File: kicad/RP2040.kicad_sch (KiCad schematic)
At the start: 22 parts, among them J1 503398-1892, SW1 side-button, SW2 SKRPADE010, U2 RP2040

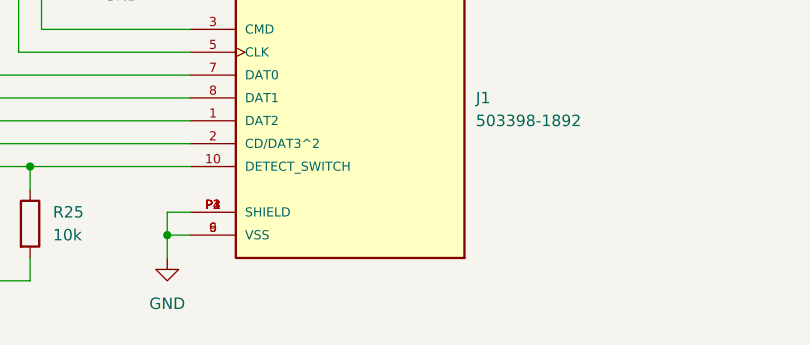
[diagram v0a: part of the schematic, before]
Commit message: added title to all circuit diagrams and sub-circuit diagrams, and PDF export
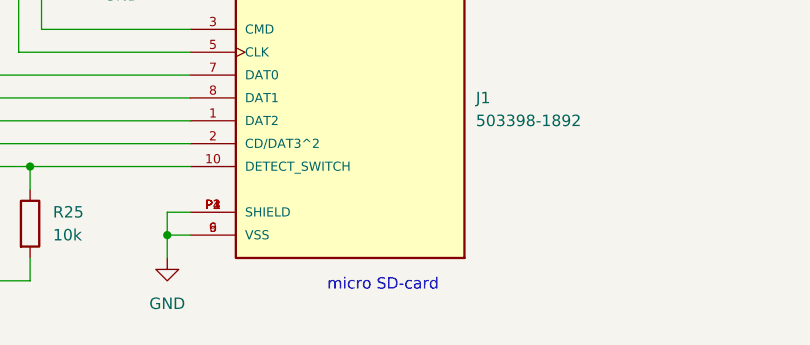
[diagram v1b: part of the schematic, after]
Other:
- note added: "micro SD-card"
- title: (none) -> RP2040 microcontroller
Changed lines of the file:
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@@
 (kicad_sch (version 20211123) (generator eeschema)
   (paper "A4")
+  (title_block
+    (title "RP2040 microcontroller")
+  )
   (junction (at 161.29 59.69) (diameter 0) (color 0 0 0 0)
   )
@@
     (stroke (width 0) (type default) (color 0 0 0 0))
   )
+  (text "micro SD-card" (at 205.74 152.4 0)
+    (effects (font (size 1.27 1.27)) (justify left bottom))
+  )
   (label "1.1V" (at 190.5 59.69 0)

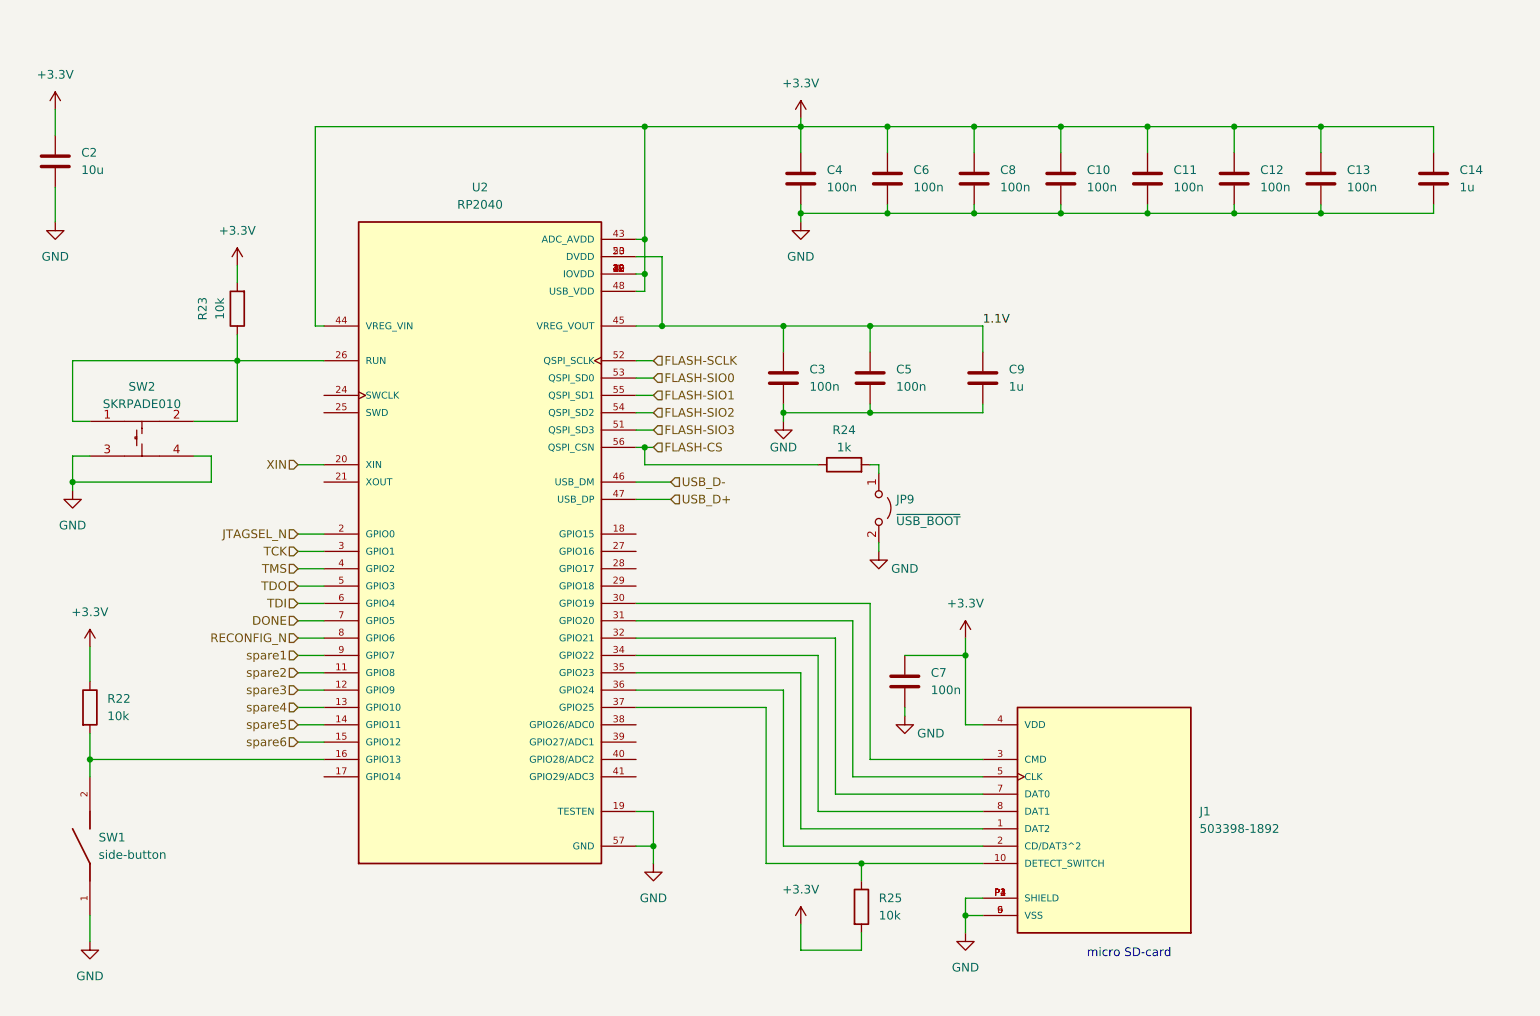
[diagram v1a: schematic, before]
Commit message: new flash, and IEC interface added
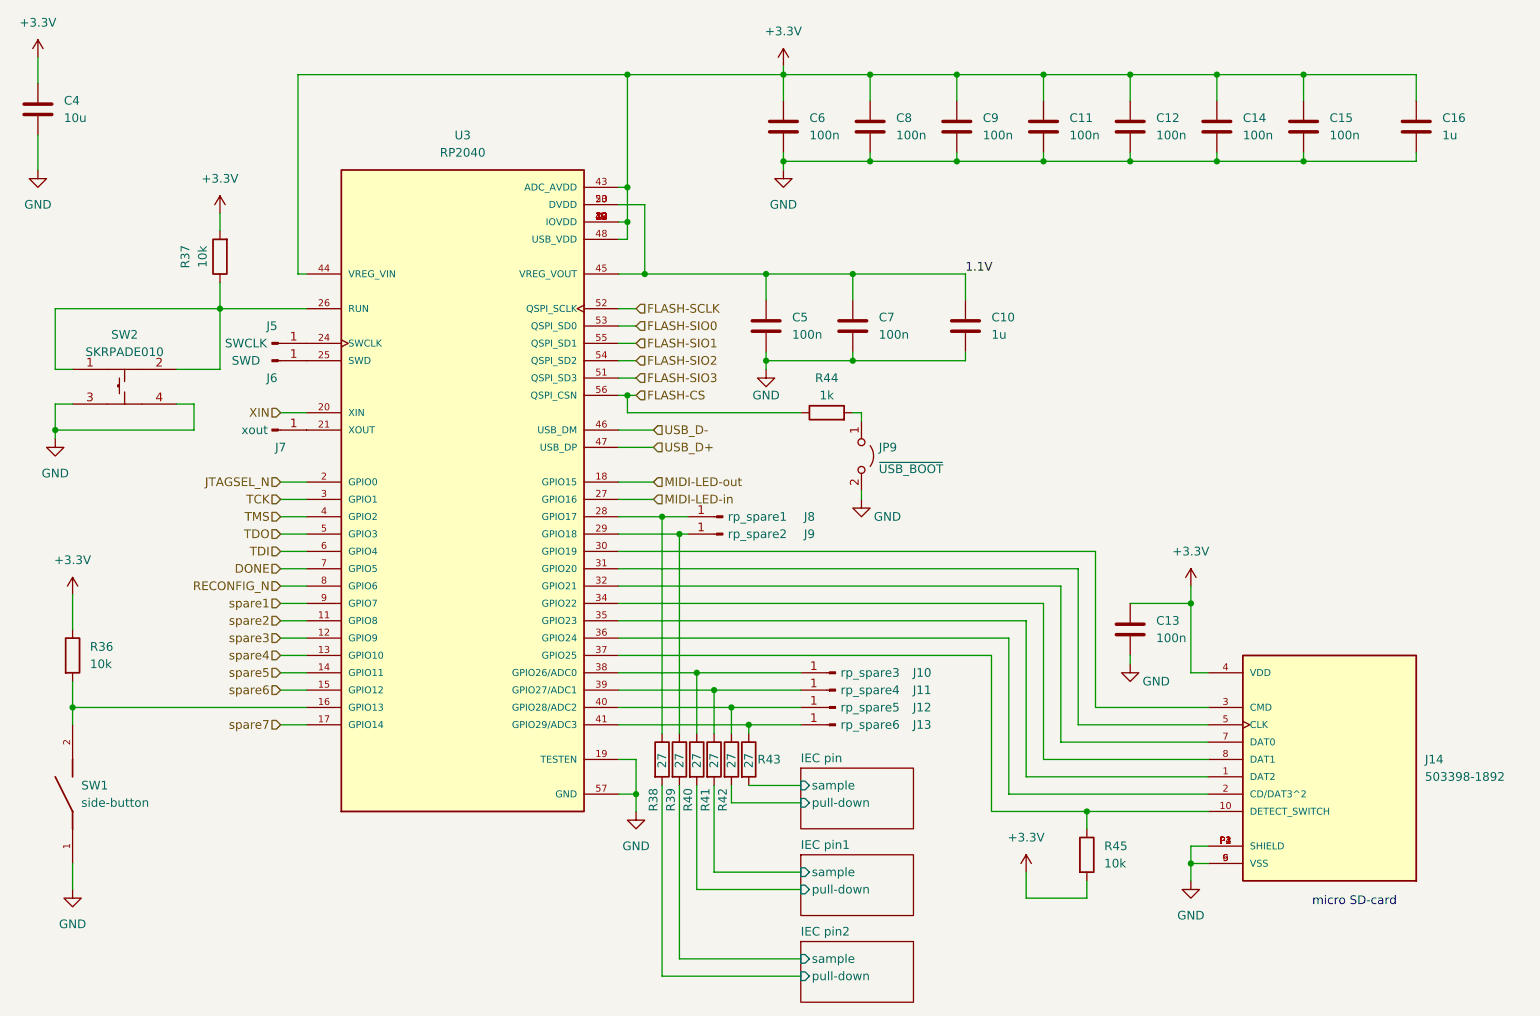
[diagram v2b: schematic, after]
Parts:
- added J10: rp_spare3, Connector_PinHeader_2.54mm:PinHeader_1x01_P2.54mm_Vertical, symbol Connector:Conn_01x01_Male
- added J11: rp_spare4, Connector_PinHeader_2.54mm:PinHeader_1x01_P2.54mm_Vertical, symbol Connector:Conn_01x01_Male
- added J12: rp_spare5, Connector_PinHeader_2.54mm:PinHeader_1x01_P2.54mm_Vertical, symbol Connector:Conn_01x01_Male
- added J13: rp_spare6, Connector_PinHeader_2.54mm:PinHeader_1x01_P2.54mm_Vertical, symbol Connector:Conn_01x01_Male
- added J5: SWCLK, Connector_PinHeader_2.54mm:PinHeader_1x01_P2.54mm_Vertical, symbol Connector:Conn_01x01_Male
- added J6: SWD, Connector_PinHeader_2.54mm:PinHeader_1x01_P2.54mm_Vertical, symbol Connector:Conn_01x01_Male
- added J7: xout, Connector_PinHeader_2.54mm:PinHeader_1x01_P2.54mm_Vertical, symbol Connector:Conn_01x01_Male
- added J8: rp_spare1, Connector_PinHeader_2.54mm:PinHeader_1x01_P2.54mm_Vertical, symbol Connector:Conn_01x01_Male
- added J9: rp_spare2, Connector_PinHeader_2.54mm:PinHeader_1x01_P2.54mm_Vertical, symbol Connector:Conn_01x01_Male
- added R38, R39, R40, R41, R42, R43: 27, Resistor_SMD:R_0805_2012Metric, symbol Device:R
- renumbered C9 to C10, C10 to C11, C11 to C12, C7 to C13, C12 to C14, C13 to C15, C14 to C16, C2 to C4, C3 to C5, C4 to C6, C5 to C7, C6 to C8, C8 to C9, J1 to J14, R22 to R36, R23 to R37, R24 to R44, R25 to R45, U2 to U3
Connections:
- net spare7: now reaches U3.17 (GPIO14)
- net MIDI-LED-out: now reaches U3.18 (GPIO15)
- net at U3.21 (XOUT): now also J7.1 (Pin_1)
- net at U3.24 (SWCLK): now also J5.1 (Pin_1)
- net at U3.25 (SWD): now also J6.1 (Pin_1)
- net MIDI-LED-in: now reaches U3.27 (GPIO16)
- net at U3.28 (GPIO17): now also J8.1 (Pin_1), R38.1
- net at U3.29 (GPIO18): now also J9.1 (Pin_1), R39.1
- net at U3.38 (GPIO26/ADC0): now also J10.1 (Pin_1), R40.1
- net at U3.39 (GPIO27/ADC1): now also J11.1 (Pin_1), R41.1
- net at U3.40 (GPIO28/ADC2): now also J12.1 (Pin_1), R42.1
- net at U3.41 (GPIO29/ADC3): now also J13.1 (Pin_1), R43.1
- new net IEC pin/pull-down: R42.2
- new net IEC pin/sample: R43.2
- new net IEC pin1/pull-down: R40.2
- new net IEC pin1/sample: R41.2
- new net IEC pin2/pull-down: R38.2
- new net IEC pin2/sample: R39.2
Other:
- added sheet IEC pin (iec-pin.kicad_sch)
- added sheet IEC pin1 (iec-pin.kicad_sch)
- added sheet IEC pin2 (iec-pin.kicad_sch)
- moved on the sheet: C10, C11, C12, C13, C14, C15, C16, C4, C5, C6, C7, C8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

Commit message: circuit improvements fixed the level shifter circuit, added the shield pins to the reset button, and replaced the IEC circuit with unused pins of the 16 bit level shifter, and a new 6 channel open collector driver
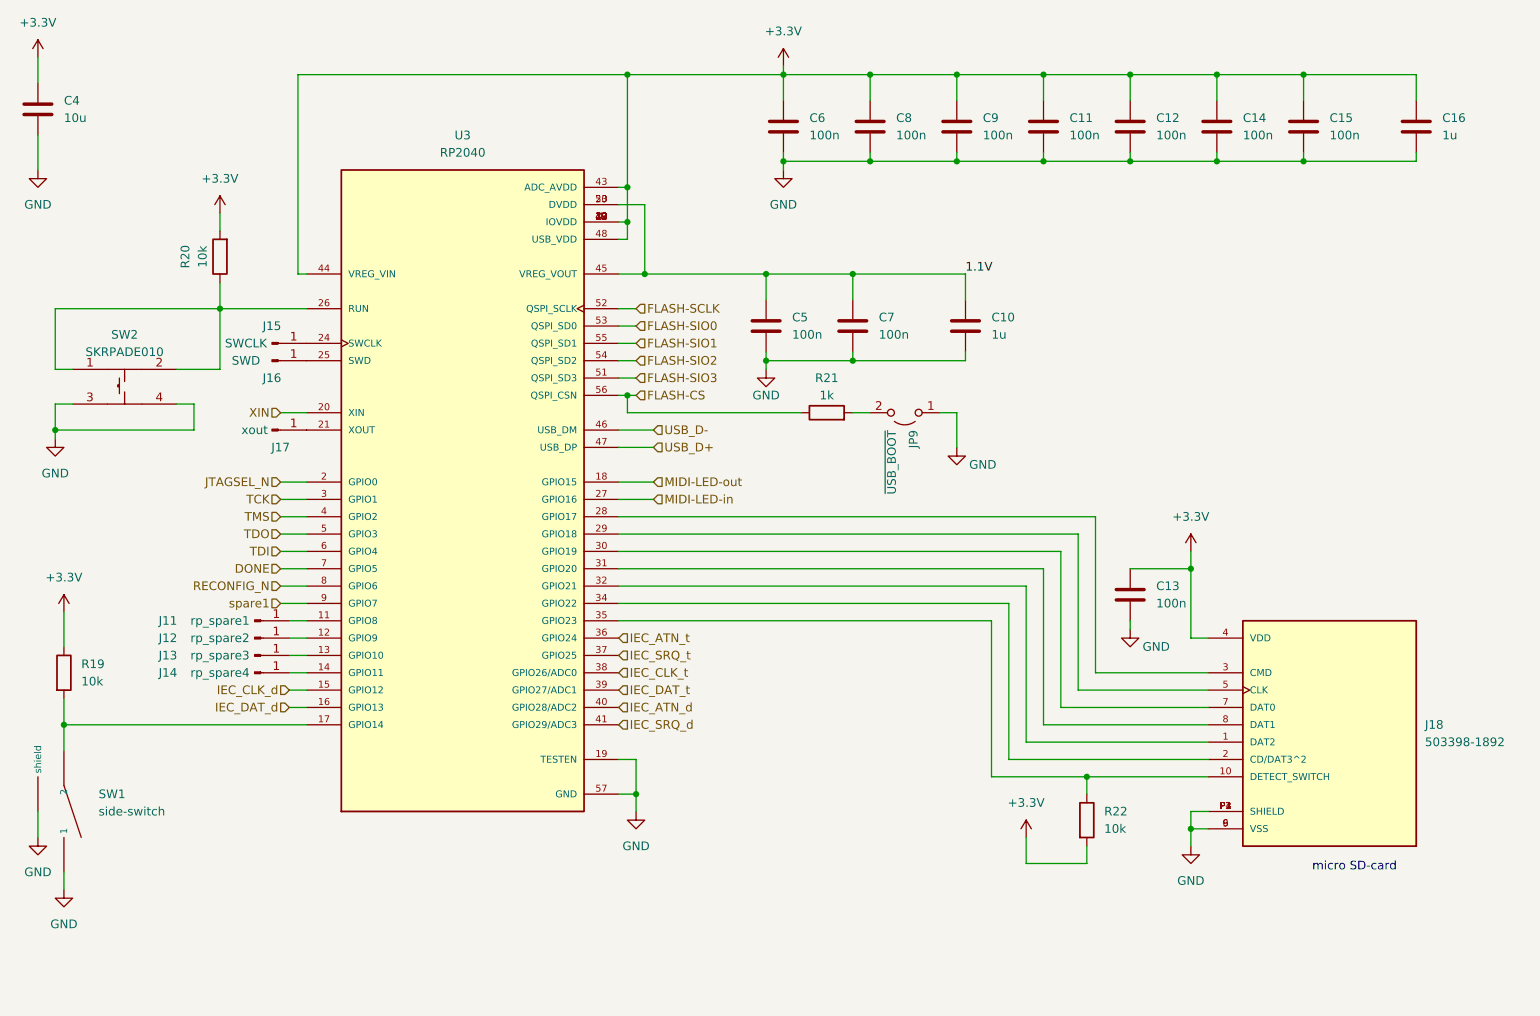
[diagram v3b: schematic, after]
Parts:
- removed J10: rp_spare3, Connector_PinHeader_2.54mm:PinHeader_1x01_P2.54mm_Vertical, symbol Connector:Conn_01x01_Male
- removed J8: rp_spare1, Connector_PinHeader_2.54mm:PinHeader_1x01_P2.54mm_Vertical, symbol Connector:Conn_01x01_Male
- removed J9: rp_spare2, Connector_PinHeader_2.54mm:PinHeader_1x01_P2.54mm_Vertical, symbol Connector:Conn_01x01_Male
- removed R38, R39, R40, R41, R42, R43: 27, Resistor_SMD:R_0805_2012Metric, symbol Device:R
- removed SW1: side-button, reset-button:SW_TL1105JAF160Q, symbol TL1105JAF160Q:TL1105JAF160Q
- added J14: rp_spare4, Connector_PinHeader_2.54mm:PinHeader_1x01_P2.54mm_Vertical, symbol Connector:Conn_01x01_Male
- added SW1: side-switch, reset-button:SW_TL1105JAF160Q, symbol side-switch:side-switch
- J11: value rp_spare4 -> rp_spare1
- J12: value rp_spare5 -> rp_spare2
- J13: value rp_spare6 -> rp_spare3
- renumbered J5 to J15, J6 to J16, J7 to J17, J14 to J18, R36 to R19, R37 to R20, R44 to R21, R45 to R22
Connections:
- net spare2 is gone; now on an unnamed net: U3.11 (GPIO8)
- net spare3 is gone; now on an unnamed net: U3.12 (GPIO9)
- net spare4 is gone; now on an unnamed net: U3.13 (GPIO10)
- net spare7 is gone; now on an unnamed net: U3.17 (GPIO14)
- net GND: now also JP9.1 (A), SW1.1, SW1.S1 (shield), SW1.S2 (shield); no longer JP9.2 (B)
- net at J11.1 (Pin_1): no longer U3.39 (GPIO27/ADC1)
- net at J18.10 (DETECT_SWITCH), R22.1: now also U3.35 (GPIO23); no longer U3.37 (GPIO25)
- net IEC_CLK_t: now reaches U3.38 (GPIO26/ADC0)
- net at J12.1 (Pin_1): no longer U3.40 (GPIO28/ADC2)
- net at R19.2: now also SW1.2; no longer U3.16 (GPIO13)
- net at U3.28 (GPIO17): now also J18.3 (CMD)
- net at U3.29 (GPIO18): now also J18.5 (CLK)
- net at U3.30 (GPIO19): now also J18.7 (DAT0); no longer J18.3 (CMD)
- net at U3.31 (GPIO20): now also J18.8 (DAT1); no longer J18.5 (CLK)
- net at U3.32 (GPIO21): now also J18.1 (DAT2); no longer J18.7 (DAT0)
- net at U3.34 (GPIO22): now also J18.2 (CD/DAT3^2); no longer J18.8 (DAT1)
- net IEC_ATN_t: now reaches U3.36 (GPIO24)
- net IEC_ATN_t: no longer J18.2 (CD/DAT3^2)
- net at J13.1 (Pin_1): no longer U3.41 (GPIO29/ADC3)
- net at R21.2: now also JP9.2 (B); no longer JP9.1 (A)
- net spare5: no longer names the net of U3.14 (GPIO11)
- net spare5: now also J14.1 (Pin_1)
- net spare6 renamed IEC_CLK_d
- new net IEC_ATN_d: U3.40 (GPIO28/ADC2)
- new net IEC_DAT_d: U3.16 (GPIO13)
- new net IEC_DAT_t: U3.39 (GPIO27/ADC1)
- new net IEC_SRQ_d: U3.41 (GPIO29/ADC3)
- new net IEC_SRQ_t: U3.37 (GPIO25)
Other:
- removed sheet IEC pin
- removed sheet IEC pin1
- removed sheet IEC pin2
- moved on the sheet: C13, J18, JP9, R19, R22

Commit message: started routing
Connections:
- net IEC_ATN_t: now also U3.38 (GPIO26/ADC0); no longer U3.36 (GPIO24)
- net IEC_CLK_t: now also U3.37 (GPIO25); no longer U3.38 (GPIO26/ADC0)
- net IEC_DAT_t: now also U3.36 (GPIO24); no longer U3.39 (GPIO27/ADC1)
- net IEC_SRQ_t: now also U3.39 (GPIO27/ADC1); no longer U3.37 (GPIO25)
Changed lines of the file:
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@@
     (effects (font (size 1.27 1.27)) (justify left))
   )
-  (hierarchical_label "IEC_CLK_t" (shape input) (at 137.16 110.49 0)
+  (hierarchical_label "IEC_CLK_t" (shape input) (at 137.16 107.95 0)
     (effects (font (size 1.27 1.27)) (justify left))
   )
@@
     (effects (font (size 1.27 1.27)) (justify right))
   )
-  (hierarchical_label "IEC_DAT_t" (shape input) (at 137.16 113.03 0)
+  (hierarchical_label "IEC_DAT_t" (shape input) (at 137.16 105.41 0)
     (effects (font (size 1.27 1.27)) (justify left))
   )
-  (hierarchical_label "IEC_SRQ_t" (shape input) (at 137.16 107.95 0)
+  (hierarchical_label "IEC_SRQ_t" (shape input) (at 137.16 113.03 0)
     (effects (font (size 1.27 1.27)) (justify left))
   )
@@
     (effects (font (size 1.27 1.27)) (justify left))
   )
-  (hierarchical_label "IEC_ATN_t" (shape input) (at 137.16 105.41 0)
+  (hierarchical_label "IEC_ATN_t" (shape input) (at 137.16 110.49 0)
     (effects (font (size 1.27 1.27)) (justify left))
   )
